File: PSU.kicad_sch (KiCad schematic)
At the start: 21 parts, among them U11 LM66200DRLR, U7 TPS631000DRLR, U8 INA232AIDDFR

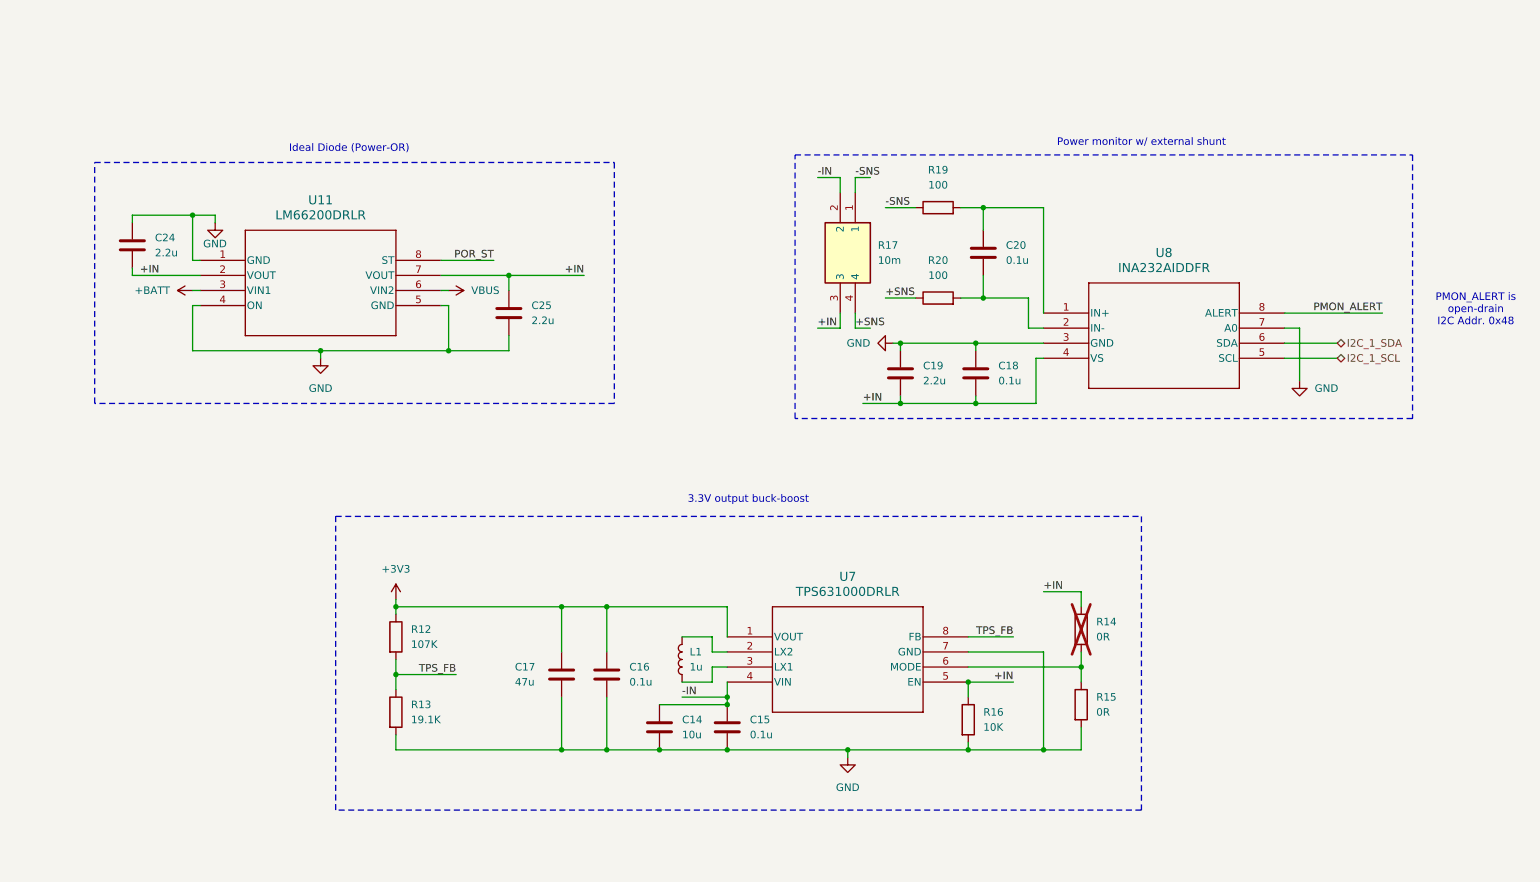
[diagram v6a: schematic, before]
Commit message: Fixed PSU, routed
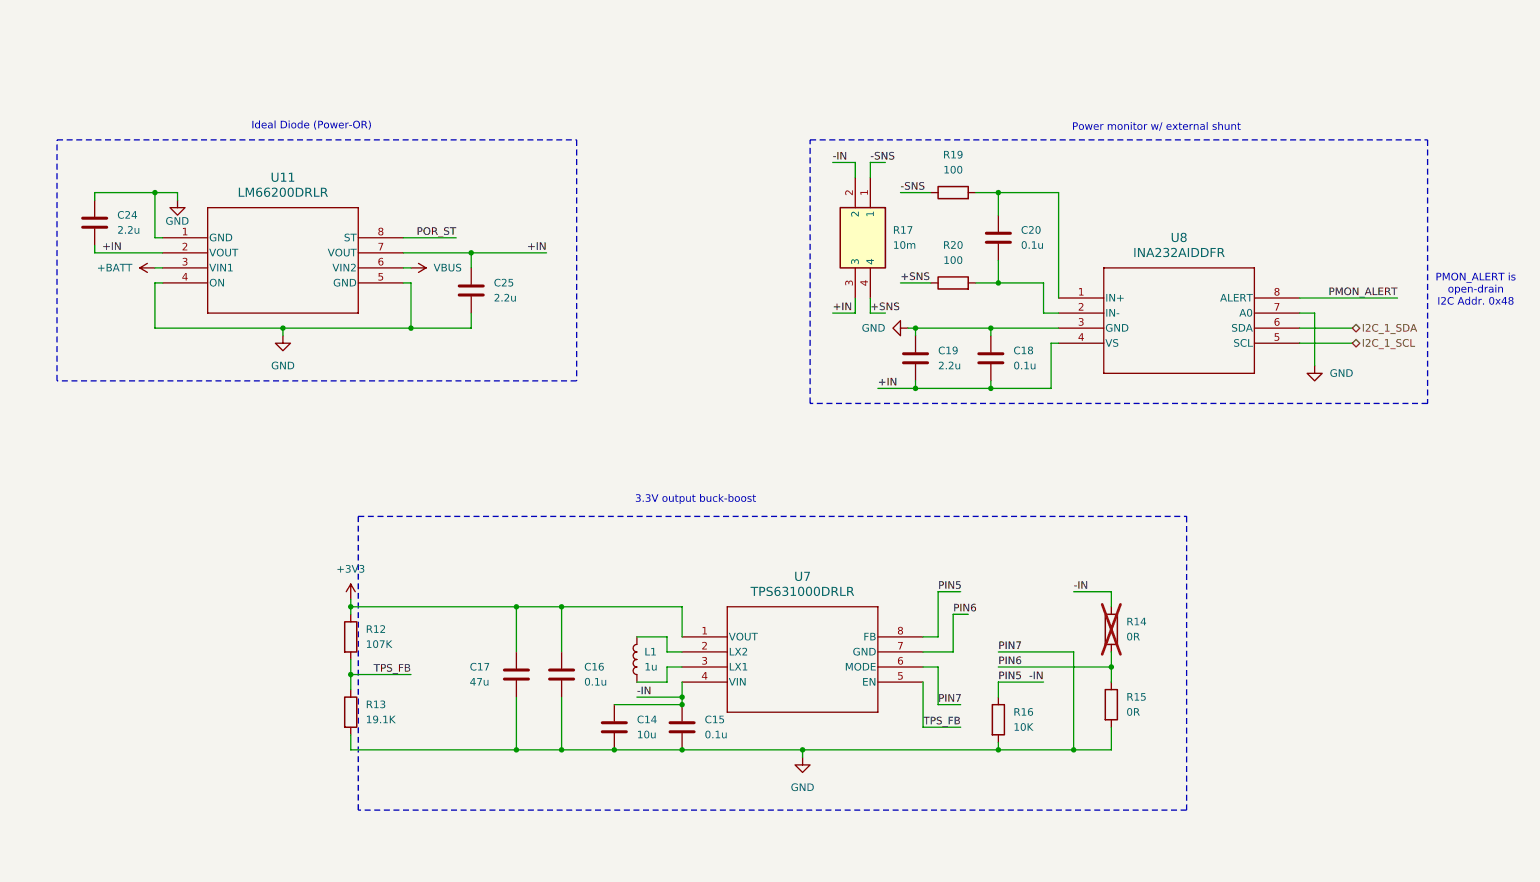
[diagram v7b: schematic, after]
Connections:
- net +IN: no longer R14.1, R16.1, U7.5 (EN)
- net -IN: now also R14.1, R16.1, U7.8 (FB)
- net GND: now also U7.6 (MODE); no longer U7.7 (GND)
- net TPS_FB: now also U7.5 (EN); no longer U7.8 (FB)
- net PIN6: now reaches R14.2, R15.1
- net PIN6: now also U7.7 (GND); no longer U7.6 (MODE)
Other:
- moved on the sheet: C14, C15, C16, C17, C18, C19, C20, C24, C25, L1, R12, R13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

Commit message: Silkscreen finished
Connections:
- net -IN: now also U7.5 (EN); no longer U7.8 (FB)
- net GND: now also U7.7 (GND); no longer U7.6 (MODE)
- net TPS_FB: now also U7.8 (FB); no longer U7.5 (EN)
- net PIN6: no longer names the net of R14.2, R15.1
- net PIN6: now also U7.6 (MODE); no longer U7.7 (GND)
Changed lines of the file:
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@@
-	)
-	(junction
-		(at 196.85 140.97)
-		(diameter 0)
-		(color 0 0 0 0)
 	)
 	(junction
@@
 	)
 	(junction
+		(at 184.15 129.54)
+		(diameter 0)
+		(color 0 0 0 0)
+	)
+	(junction
 		(at 110.49 140.97)
 		(diameter 0)
@@
 		(color 0 0 0 0)
 	)
-	(wire
-		(pts
-			(xy 196.85 124.46) (xy 196.85 140.97)
-		)
-		(stroke
-			(width 0)
-			(type default)
-		)
+	(junction
+		(at 175.26 140.97)
+		(diameter 0)
+		(color 0 0 0 0)
 	)
 	(wire
@@
 	(wire
 		(pts
-			(xy 173.99 114.3) (xy 173.99 121.92)
-		)
-		(stroke
-			(width 0)
-			(type default)
-		)
-	)
-	(wire
-		(pts
-			(xy 196.85 140.97) (xy 184.15 140.97)
+			(xy 184.15 140.97) (xy 203.2 140.97)
 		)
 		(stroke
@@
 	(wire
 		(pts
-			(xy 171.45 137.16) (xy 177.8 137.16)
+			(xy 171.45 129.54) (xy 184.15 129.54)
 		)
 		(stroke
@@
 	(wire
 		(pts
-			(xy 176.53 118.11) (xy 179.07 118.11)
+			(xy 184.15 129.54) (xy 191.77 129.54)
 		)
 		(stroke
@@
 	(wire
 		(pts
-			(xy 151.13 140.97) (xy 184.15 140.97)
+			(xy 151.13 140.97) (xy 175.26 140.97)
 		)
 		(stroke
@@
 	(wire
 		(pts
+			(xy 175.26 124.46) (xy 175.26 140.97)
+		)
+		(stroke
+			(width 0)
+			(type default)
+		)
+	)
+	(wire
+		(pts
 			(xy 151.13 140.97) (xy 151.13 142.24)
 		)
@@
 	(wire
 		(pts
-			(xy 184.15 124.46) (xy 196.85 124.46)
-		)
-		(stroke
-			(width 0)
-			(type default)
-		)
-	)
-	(wire
-		(pts
 			(xy 203.2 114.3) (xy 196.85 114.3)
 		)
@@
 	(wire
 		(pts
-			(xy 176.53 118.11) (xy 176.53 124.46)
-		)
-		(stroke
-			(width 0)
-			(type default)
-		)
-	)
-	(wire
-		(pts
 			(xy 45.72 48.26) (xy 45.72 46.99)
 		)
@@
 	(wire
 		(pts
-			(xy 173.99 114.3) (xy 177.8 114.3)
-		)
-		(stroke
-			(width 0)
-			(type default)
-		)
-	)
-	(wire
-		(pts
 			(xy 182.88 80.01) (xy 193.04 80.01)
 		)
@@
 	(wire
 		(pts
-			(xy 171.45 127) (xy 173.99 127)
+			(xy 184.15 129.54) (xy 184.15 132.08)
+		)
+		(stroke
+			(width 0)
+			(type default)
+		)
+	)
+	(wire
+		(pts
+			(xy 171.45 127) (xy 203.2 127)
 		)
 		(stroke
@@
 	(wire
 		(pts
-			(xy 173.99 127) (xy 173.99 133.35)
-		)
-		(stroke
-			(width 0)
-			(type default)
-		)
-	)
-	(wire
-		(pts
 			(xy 128.27 127) (xy 128.27 129.54)
 		)
@@
 	(wire
 		(pts
-			(xy 184.15 129.54) (xy 191.77 129.54)
-		)
-		(stroke
-			(width 0)
-			(type default)
-		)
-	)
-	(wire
-		(pts
 			(xy 203.2 116.84) (xy 203.2 114.3)
 		)
@@
 	(wire
 		(pts
-			(xy 184.15 127) (xy 203.2 127)
-		)
-		(stroke
-			(width 0)
-			(type default)
-		)
-	)
-	(wire
-		(pts
 			(xy 85.09 69.85) (xy 95.25 69.85)
 		)
@@
 	(wire
 		(pts
-			(xy 184.15 129.54) (xy 184.15 132.08)
-		)
-		(stroke
-			(width 0)
-			(type default)
-		)
-	)
-	(wire
-		(pts
 			(xy 237.49 76.2) (xy 237.49 67.31)
 		)
@@
 	(wire
 		(pts
-			(xy 173.99 133.35) (xy 177.8 133.35)
+			(xy 175.26 140.97) (xy 184.15 140.97)
 		)
 		(stroke
@@
 	(wire
 		(pts
-			(xy 196.85 140.97) (xy 203.2 140.97)
-		)
-		(stroke
-			(width 0)
-			(type default)
-		)
-	)
-	(wire
-		(pts
 			(xy 74.93 140.97) (xy 102.87 140.97)
 		)
@@
 	(wire
 		(pts
-			(xy 171.45 129.54) (xy 171.45 137.16)
-		)
-		(stroke
-			(width 0)
-			(type default)
-		)
-	)
-	(wire
-		(pts
 			(xy 184.15 46.99) (xy 194.31 46.99)
 		)
@@
 	(wire
 		(pts
-			(xy 171.45 124.46) (xy 176.53 124.46)
+			(xy 171.45 124.46) (xy 175.26 124.46)
 		)
 		(stroke
@@
 	(wire
 		(pts
-			(xy 171.45 121.92) (xy 173.99 121.92)
+			(xy 171.45 121.92) (xy 185.42 121.92)
 		)
 		(stroke
@@
 	)
 	(rectangle
-		(start 76.2 101.6)
-		(end 215.9 151.13)
+		(start 67.31 101.6)
+		(end 214.63 151.13)
 		(stroke
 			(width 0)
@@
 		)
 	)
-	(label "PIN6"
-		(at 184.15 127 0)
-		(fields_autoplaced yes)
-		(effects
-			(font
-				(size 1.27 1.27)
-			)
-			(justify left bottom)
+	(label "TPS_FB"
+		(at 185.42 121.92 180)
+		(fields_autoplaced yes)
+		(effects
+			(font
+				(size 1.27 1.27)
+			)
+			(justify right bottom)
 		)
 	)
@@
 		)
 	)
-	(label "PIN5"
-		(at 173.99 114.3 0)
-		(fields_autoplaced yes)
-		(effects
-			(font
-				(size 1.27 1.27)
-			)
-			(justify left bottom)
-		)
-	)
-	(label "PIN7"
-		(at 184.15 124.46 0)
-		(fields_autoplaced yes)
-		(effects
-			(font
-				(size 1.27 1.27)
-			)
-			(justify left bottom)
-		)
-	)
 	(label "+IN"
 		(at 156.21 67.31 0)
@@
 		)
 	)
-	(label "PIN7"
-		(at 173.99 133.35 0)
-		(fields_autoplaced yes)
-		(effects
-			(font
-				(size 1.27 1.27)
-			)
-			(justify left bottom)
-		)
-	)
-	(label "TPS_FB"
-		(at 177.8 137.16 180)
-		(fields_autoplaced yes)
-		(effects
-			(font
-				(size 1.27 1.27)
-			)
-			(justify right bottom)
-		)
-	)
 	(label "+IN"
 		(at 163.83 80.01 0)
@@
 		)
 	)
-	(label "PIN5"
-		(at 184.15 129.54 0)
-		(fields_autoplaced yes)
-		(effects
-			(font
-				(size 1.27 1.27)
-			)
-			(justify left bottom)
-		)
-	)
 	(label "+SNS"
 		(at 162.56 67.31 0)
@@
 		(fields_autoplaced yes)
 		(effects
-			(font
-				(size 1.27 1.27)
-			)
-			(justify left bottom)
-		)
-	)
-	(label "PIN6"
-		(at 176.53 118.11 0)
-		(fields_autoplaced yes)
-		(effects
